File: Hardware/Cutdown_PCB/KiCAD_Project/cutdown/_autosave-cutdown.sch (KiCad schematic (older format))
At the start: 64 parts, among them J1 Mini_USB_B, J3 External Cutdown, J4 ISP, Q1 2N7002, SW1 SW_SPST, U1 FT231XS, U2 SPX3819M5-L-3-3, U3 ATmega328P-AU, U5 XBee, Y1 8MHz

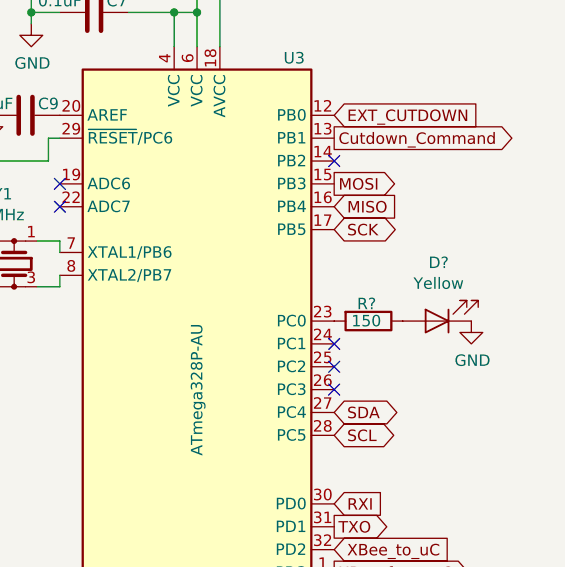
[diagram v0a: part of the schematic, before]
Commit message: Move batteries, remove charging circuit, add mounting holes.
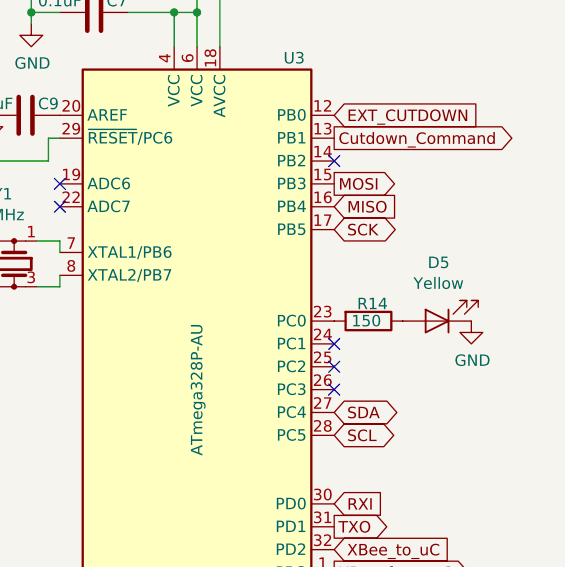
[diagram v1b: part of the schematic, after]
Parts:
- gave numbers to parts that had none: 2
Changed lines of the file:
@@
 Connection ~ 2325 3500
 $Comp
-L resistors_0603:1-0000008 R?
+L resistors_0603:1-0000008 R14
 U 1 1 618DC6D0
 P 10375 3925
-F 0 "R?" V 10300 3875 50  0000 L CNN
+F 0 "R14" V 10300 3875 50  0000 L CNN
 F 1 "1-0000008" V 10375 3925 50  0001 C CNN
 F 2 "resistors_0603:1-0000008" V 10305 3925 50  0001 C CNN
@@
 $EndComp
 $Comp
-L leds_0805:1-0000601 D?
+L leds_0805:1-0000601 D5
 U 1 1 618DDD37
 P 10675 3925
-F 0 "D?" H 10668 3670 50  0000 C CNN
+F 0 "D5" H 10668 3670 50  0000 C CNN
 F 1 "1-0000601" H 10675 3825 50  0001 C CNN
 F 2 "leds_0805:1-0000601" H 10675 3925 50  0001 C CNN
@@
 $EndComp
 $Comp
-L power:GND #PWR?
+L power:GND #PWR022
 U 1 1 618DEED9
 P 10825 3925
-F 0 "#PWR?" H 10825 3675 50  0001 C CNN
+F 0 "#PWR022" H 10825 3675 50  0001 C CNN
 F 1 "GND" H 10830 3752 50  0000 C CNN
 F 2 "" H 10825 3925 50  0001 C CNN
